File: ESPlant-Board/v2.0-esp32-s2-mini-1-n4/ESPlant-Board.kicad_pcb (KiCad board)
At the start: 2 copper layers, 22 x 127 mm, 39 parts, among them J1 Conn_01x05, U1 ESP32-S2-MINI-1-N4, U3 Reset, U4 Boot, U5 Temp/Humid-Sensor, U6 Light sensor, U7 AMS1117-3_3, U8 MK-12C02-G025

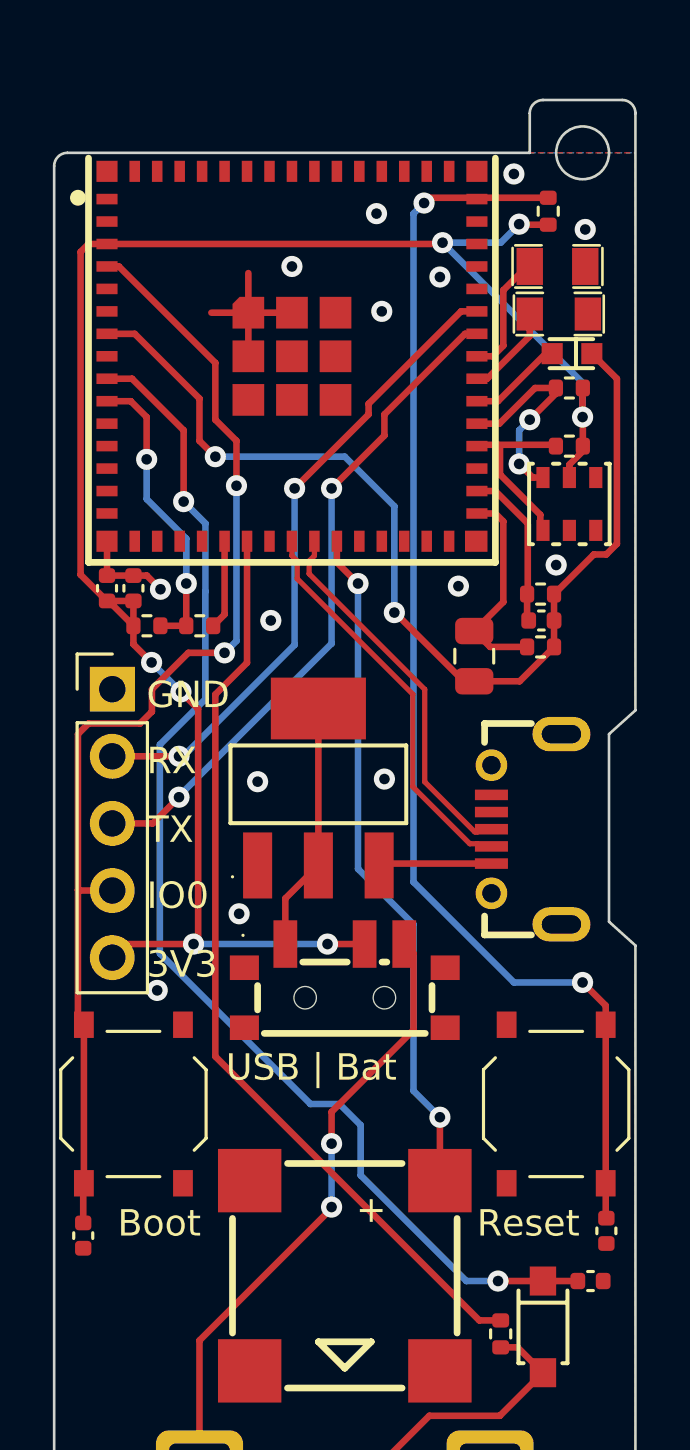
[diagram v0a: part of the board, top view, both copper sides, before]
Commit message: Case: Add v2 case with improved folder structure
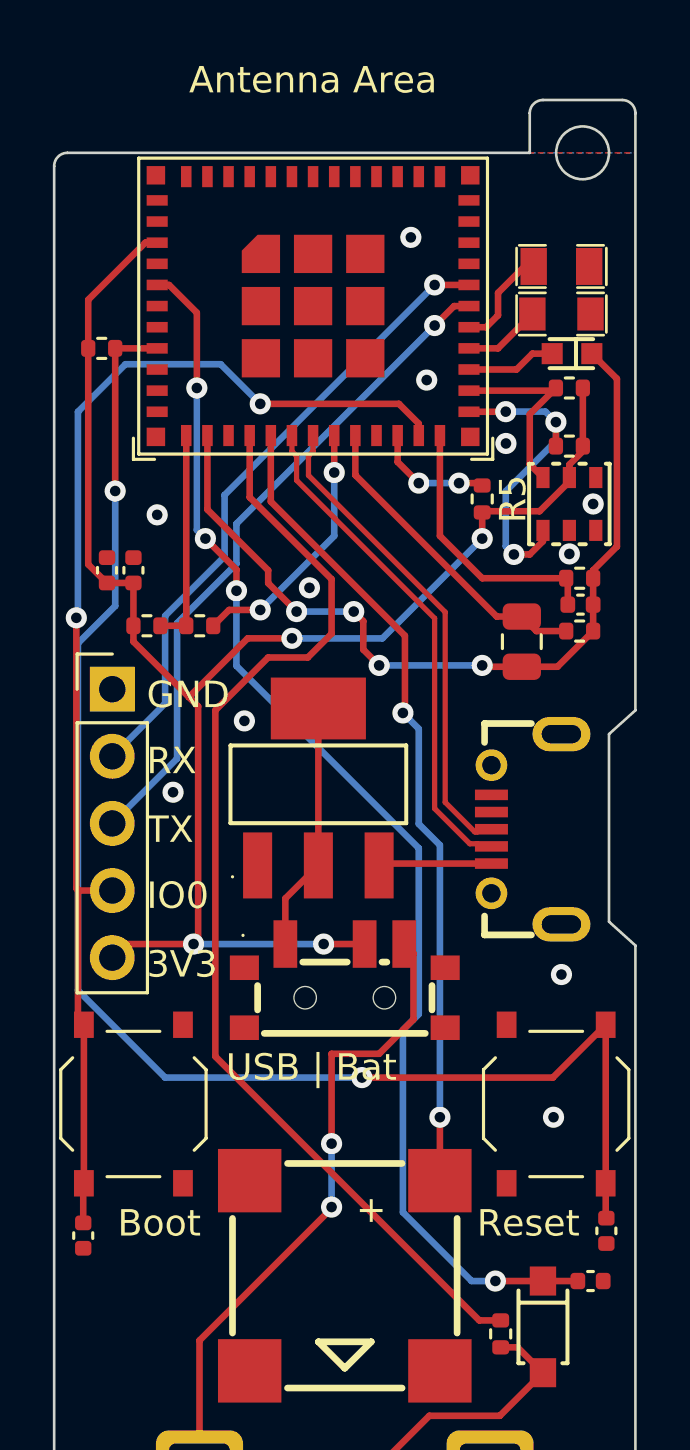
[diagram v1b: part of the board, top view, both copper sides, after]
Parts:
- removed the REF** at (254.9, 163.2)
- removed the REF** at (259.9, 136.1)
- removed the REF** at (237.1, 136.1)
- removed the REF** at (259.9, 118.3)
- removed the REF** at (259.9, 147.1)
- removed the REF** at (237.1, 147.1)
- removed the REF** at (242.1, 163.2)
- removed the REF** at (237.1, 118.3)
- removed the REF** at (237.1, 103.5)
- added R5: 10k, Resistor_SMD:R_0402_1005Metric, F.Cu at (253.7, 113.1)
- added REF**: Tab_5mm, PCM_kikit:Tab_5mm, F.Cu at (237.2, 146.8)
- added REF**: Tab_5mm, PCM_kikit:Tab_5mm, F.Cu at (260.0, 146.8)
- added REF**: Tab_5mm, PCM_kikit:Tab_5mm, F.Cu at (237.2, 103.5)
- added REF**: Tab_5mm, PCM_kikit:Tab_5mm, F.Cu at (260.0, 118.3)
- added REF**: Tab_5mm, PCM_kikit:Tab_5mm, F.Cu at (237.1, 118.3)
- U1: value ESP32-S2-MINI-1-N4 -> ESP32-C6-MINI-1/U; footprint CustomFootprints:WIFI-SMD_ESP32-MINI-1-N4 -> Espressif:ESP32-C6-MINI-1
- moved R9 17.7 mm to (239.3, 107.4), turned to 0 degrees
- moved U1 4.67 mm to (247.3, 103.1)
- moved C7 1.88 mm to (255.2, 118.5)
- moved R1 1.60 mm to (257.4, 116.1)
- moved R3 1.60 mm to (257.4, 118.1)
- moved C5 1.60 mm to (257.5, 117.1)
- moved C8 0.68 mm to (240.5, 115.8)
- moved C9 0.68 mm to (239.5, 115.8)
- moved D1 0.15 mm to (256.7, 104.3)
- moved D3 0.10 mm to (256.7, 106.1)
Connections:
- C2 pad 2: /IO0 -> /IO9
- J1 pad 2: /RX -> /TX
- J1 pad 3: /TX -> /RX
- J1 pad 4: /IO0 -> /IO9
- R9 pad 1: /EN -> +3V3
- R9 pad 2: +3V3 -> /EN
- U1 pad 10: /Voltage_Measurement_Analog -> unconnected-(U1-MTDI/GPIO5/ADC1_CH5-Pad10)
- U1 pad 11: unconnected-(U1-IO7-Pad11) -> GND
- U1 pad 12: unconnected-(U1-IO8-Pad12) -> /Voltage_Measurement_Analog
- U1 pad 13: unconnected-(U1-IO9-Pad13) -> /Light_Sensor_Analog
- U1 pad 14: unconnected-(U1-IO10-Pad14) -> GND
- U1 pad 15: unconnected-(U1-IO11-Pad15) -> /Square_Wave_Signal
- U1 pad 16: unconnected-(U1-IO12-Pad16) -> /Buzzer
- U1 pad 17: unconnected-(U1-IO13-Pad17) -> /D-
- U1 pad 18: unconnected-(U1-IO14-Pad18) -> /D+
- U1 pad 19: unconnected-(U1-IO15-Pad19) -> /Voltage_Measurement_Select
- U1 pad 20: /Voltage_Measurement_Select -> /Light_Sensor_Select_2
- U1 pad 21: /Square_Wave_Signal -> unconnected-(U1-NC-Pad21)
- U1 pad 22: unconnected-(U1-IO18-Pad22) -> /IO8
- U1 pad 23: /D- -> /IO9
- U1 pad 24: /D+ -> /Light_Sensor_Select_1
- U1 pad 25: /Buzzer -> /TH_SDA
- U1 pad 26: unconnected-(U1-IO26-Pad26) -> /TH_SCL
- U1 pad 27: unconnected-(U1-NC-Pad27) -> /Light_Sensor_In
- U1 pad 28: unconnected-(U1-IO33-Pad28) -> /LED_RED
- U1 pad 29: unconnected-(U1-IO34-Pad29) -> /LED_GREEN
- U1 pad 30: GND -> /RX
- U1 pad 31: /Light_Sensor_Select_2 -> /TX
- U1 pad 32: /Light_Sensor_Select_1 -> unconnected-(U1-NC-Pad32)
- U1 pad 34: /TH_SDA -> unconnected-(U1-NC-Pad34)
- U1 pad 35: /TH_SCL -> unconnected-(U1-NC-Pad35)
- U1 pad 36: /Light_Sensor_In -> GND
- U1 pad 37: /LED_RED -> GND
- U1 pad 38: /LED_GREEN -> GND
- U1 pad 39: /TX -> GND
- U1 pad 4: /IO0 -> unconnected-(U1-NC-Pad4)
- U1 pad 40: /RX -> GND
- U1 pad 41: unconnected-(U1-IO45-Pad41) -> GND
- U1 pad 44: unconnected-(U1-IO46-Pad44) -> GND
- U1 pad 45: /EN -> GND
- U1 pad 5: unconnected-(U1-IO1-Pad5) -> /AD_Capacitance
- U1 pad 7: /Light_Sensor_Analog -> unconnected-(U1-NC-Pad7)
- U1 pad 8: unconnected-(U1-IO4-Pad8) -> /EN
- U1 pad 9: /AD_Capacitance -> unconnected-(U1-MTMS/GPIO4/ADC1_CH4-Pad9)
- U4 pad 2: /IO0 -> /IO9
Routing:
- net /IO9: track 0.00 -> 47.2 mm, vias 0 -> 2
- net /IO0: track 44.3 -> 0.00 mm, vias 2 -> 0
- net GND: track 9.77 -> 0.04 mm, vias 17 -> 14
- net +3V3: track 70.4 -> 62.1 mm, vias 7 -> 4
- net /EN: track 47.9 -> 56.0 mm
- net /Square_Wave_Signal: track 34.9 -> 42.4 mm
- net /Voltage_Measurement_Select: track 3.38 -> 9.79 mm, vias 0 -> 2
- net /Light_Sensor_Analog: track 39.0 -> 32.6 mm, vias 2 -> 4
- net /TH_SDA: track 6.93 -> 12.0 mm, vias 0 -> 3
- net /Buzzer: track 25.9 -> 30.9 mm
- net /IO8: track 0.00 -> 4.57 mm, vias 0 -> 2
- net /Light_Sensor_Select_1: track 6.14 -> 10.3 mm
- net /D+: track 14.4 -> 18.4 mm
- net /D-: track 15.1 -> 19.1 mm
- net /Light_Sensor_Select_2: track 7.98 -> 11.9 mm
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
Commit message: Finish v2.0 for prototyping
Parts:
- moved REF** 137.5 mm to (99.7, 103.9)
- moved REF** 137.5 mm to (122.4, 103.9)
- moved REF** 137.5 mm to (122.5, 146.5)
- moved REF** 137.5 mm to (122.5, 118.0)
- moved REF** 137.5 mm to (99.5, 118.0)
- moved REF** 137.5 mm to (99.7, 146.5)
- moved U1 137.5 mm to (109.8, 103.2)
- moved C7 137.5 mm to (117.7, 118.5)
- moved D1 137.5 mm to (119.2, 104.3)
- moved D2 137.5 mm to (118.5, 144.4)
- moved D3 137.5 mm to (119.2, 106.1)
- moved J1 137.5 mm to (102.2, 120.3)
- moved R1 137.5 mm to (119.9, 116.1)
- moved R10 137.5 mm to (119.5, 111.1)
- moved R2 137.5 mm to (119.5, 108.9)
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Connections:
- net Net-(U7-VOUT-Pad2) renamed /USB
- net Net-(U9-+) renamed /BAT
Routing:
- net +3V3: track 62.1 -> 62.7 mm
- net /IO9: track 47.2 -> 47.7 mm
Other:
- board text added: "IO9"
- board text removed: "IO0"
